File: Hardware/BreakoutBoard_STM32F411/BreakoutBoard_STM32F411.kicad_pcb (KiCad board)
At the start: 2 copper layers, 38 parts, among them IC101 STM32F411CCU6TR, IC401 TLV77333PDBVR, IC402 TLV77333PDBVR, J201 GSB1C41110SSHR, J202 PortB1, J203 PortB2, J204 PortA1, J205 PortA2, J206 SPI2, J207 PortA1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

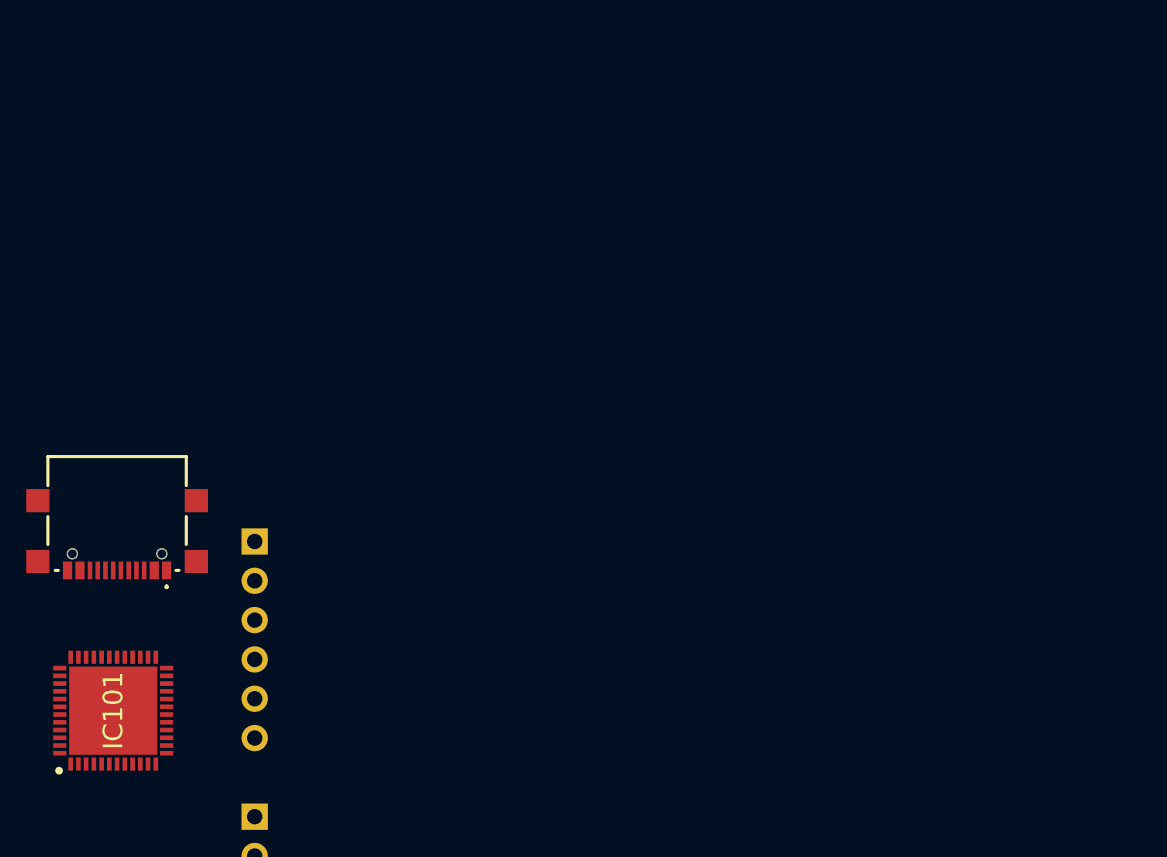
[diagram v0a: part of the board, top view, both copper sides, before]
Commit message: edited: default design rules
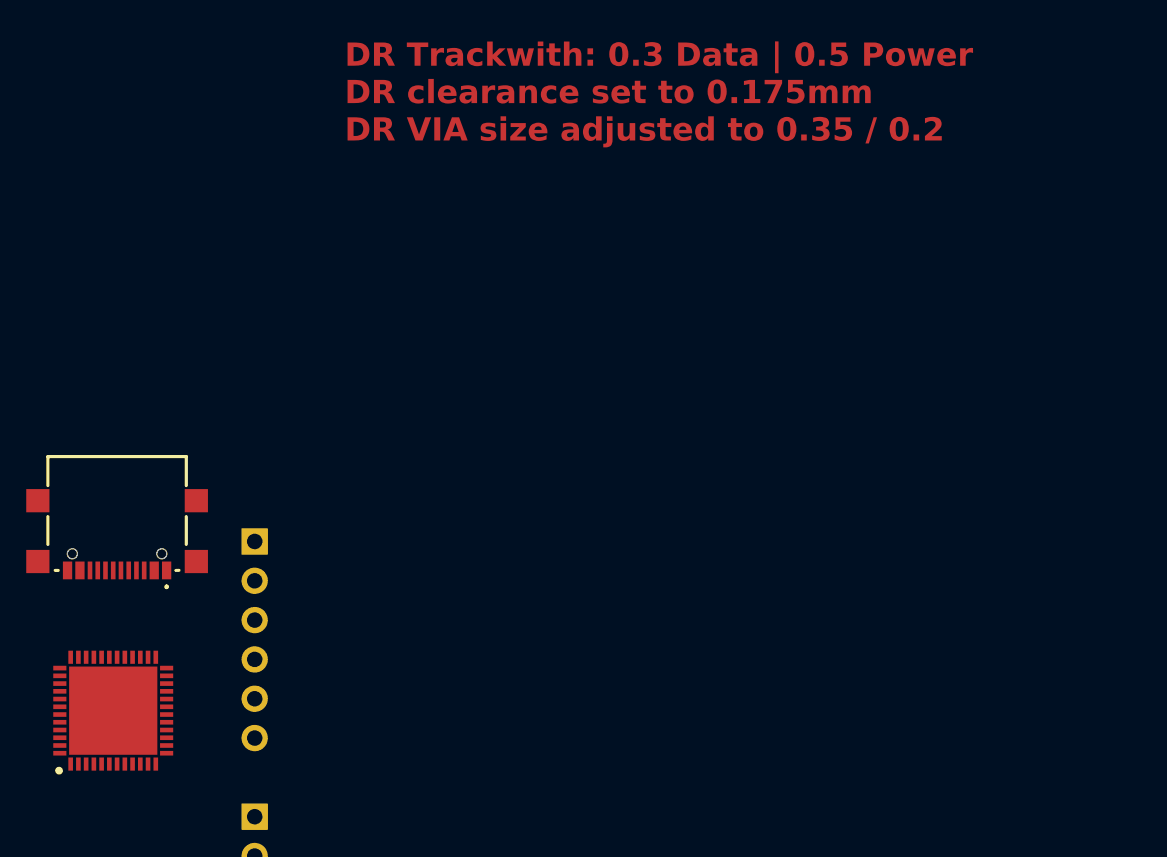
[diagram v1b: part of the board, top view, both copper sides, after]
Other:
- board text added: "DR Trackwith: 0.3 Data | 0.5 Power DR clearance set to 0.175mm DR VIA size adjusted to 0.35 / 0.2"
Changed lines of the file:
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@@
 	)
 	(setup
+		(stackup
+			(layer "F.SilkS"
+				(type "Top Silk Screen")
+			)
+			(layer "F.Paste"
+				(type "Top Solder Paste")
+			)
+			(layer "F.Mask"
+				(type "Top Solder Mask")
+				(thickness 0.01)
+			)
+			(layer "F.Cu"
+				(type "copper")
+				(thickness 0.035)
+			)
+			(layer "dielectric 1"
+				(type "core")
+				(thickness 1.51)
+				(material "FR4")
+				(epsilon_r 4.5)
+				(loss_tangent 0.02)
+			)
+			(layer "B.Cu"
+				(type "copper")
+				(thickness 0.035)
+			)
+			(layer "B.Mask"
+				(type "Bottom Solder Mask")
+				(thickness 0.01)
+			)
+			(layer "B.Paste"
+				(type "Bottom Solder Paste")
+			)
+			(layer "B.SilkS"
+				(type "Bottom Silk Screen")
+			)
+			(copper_finish "None")
+			(dielectric_constraints no)
+		)
 		(pad_to_mask_clearance 0)
 		(allow_soldermask_bridges_in_footprints no)
@@
 			(at 0 0 90)
 			(layer "F.SilkS")
+			(hide yes)
 			(effects
 				(font
@@
 		(layer "F.CrtYd")
 	)
+	(gr_text "DR Trackwith: 0.3 Data | 0.5 Power\nDR clearance set to 0.175mm\nDR VIA size adjusted to 0.35 / 0.2\n"
+		(at 139.7 26.8 0)
+		(layer "F.Cu")
+		(effects
+			(font
+				(size 1.5 1.5)
+				(thickness 0.3)
+				(bold yes)
+			)
+			(justify left bottom)
+		)
+	)
 	(embedded_fonts no)

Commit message: arranged:components (#3)
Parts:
- removed J206: SPI2, Connector_PinHeader_2.54mm:PinHeader_1x06_P2.54mm_Vertical
- removed J207: PortA1, Connector_PinHeader_2.54mm:PinHeader_1x06_P2.54mm_Vertical
- added J401: DeleteAfterPlacement1, Connector_PinHeader_2.54mm:PinHeader_1x06_P2.54mm_Vertical, F.Cu at (197.8, 42.9)
- added J402: DeleteAfterPlacement2, Connector_PinHeader_2.54mm:PinHeader_1x15_P2.54mm_Vertical, F.Cu at (180.8, 39.7)
- added J403: Conn_02x03_Odd_Even, Connector_PinHeader_2.54mm:PinHeader_2x03_P2.54mm_Vertical, F.Cu at (164.8, 147.9)
- added J404: SYS_JTAG, Connector_PinHeader_2.54mm:PinHeader_1x04_P2.54mm_Vertical, F.Cu at (158.4, 126.8)
- added J405: I2C2, Connector_PinHeader_2.54mm:PinHeader_1x04_P2.54mm_Vertical, B.Cu at (176.2, 126.8)
- moved LED701 134.0 mm to (166.0, 152.4)
- moved C701 131.9 mm to (166.1, 150.9)
- moved LED901 129.4 mm to (171.2, 152.4)
- moved C901 127.2 mm to (171.3, 150.9)
- moved C102 125.8 mm to (168.3, 138.1), turned to 180 degrees
- moved LED801 123.1 mm to (168.6, 152.4)
- moved C103 121.6 mm to (162.2, 139.6), turned to 90 degrees
- moved C801 120.9 mm to (168.7, 150.9)
- moved C106 118.3 mm to (171.8, 130.6), turned to -90 degrees
- moved C104 117.6 mm to (162.4, 136.3), turned to 90 degrees
- moved LED601 115.2 mm to (163.4, 152.4)
- moved Y101 113.8 mm to (165.0, 139.7)
- moved C601 112.8 mm to (163.5, 150.9)
- moved C101 111.6 mm to (168.9, 139.3)
- moved C105 111.5 mm to (172.8, 133.2), turned to 90 degrees
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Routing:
- net GND: track 0.00 -> 29.0 mm, vias 0 -> 24
- net +5V: track 0.00 -> 27.9 mm, vias 0 -> 20
- net PA11: track 0.00 -> 13.2 mm
- net +3.3V: track 0.00 -> 13.1 mm, vias 0 -> 11
- net PA12: track 0.00 -> 12.9 mm
- net DN: track 0.00 -> 9.24 mm, vias 0 -> 2
- net DP: track 0.00 -> 9.19 mm, vias 0 -> 2
- net /HMI_Debbug_4/AdrLED3/DO: track 0.00 -> 3.97 mm, vias 0 -> 2
- net /HMI_Debbug_4/AdrLED2/DO: track 0.00 -> 3.97 mm, vias 0 -> 2
- net /HMI_Debbug_4/AdrLED1/DO: track 0.00 -> 3.97 mm, vias 0 -> 2
- net Net-(IC101-VCAP_1): track 0.00 -> 2.45 mm
- net PH0: track 0.00 -> 2.33 mm
- net PA15 | TIM2_CH1: track 0.00 -> 1.25 mm, vias 0 -> 2
- net PB2: track 0.00 -> 1.10 mm, vias 0 -> 1
- net PB0: track 0.00 -> 1.10 mm, vias 0 -> 1
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- added copper zone on F.Cu, net +3.3V
- added copper zone on F.Cu, net +3.3VP
- added copper zone on F.Cu, net +5V
- added copper zone on B.Cu, net GND
- added copper zone on F.Cu, net GND
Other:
- board outline added: 21.4 x 50.1 mm
- board text added: "DR Trackwith: 0.3 Data | 0.5 Power DR clearance set to 0.175mm DR VIA size adjusted to 0.35 / 0.2 DR only using 0.1mm grid (0.5 if necessary)"
- board text added: "Die pins auf den PinHeadern gehören den umständen entsprächend getauscht!"
- board text removed: "DR Trackwith: 0.3 Data | 0.5 Power DR clearance set to 0.175mm DR VIA size adjusted to 0.35 / 0.2"

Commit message: routed PCB (#4)
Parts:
- D301: value LED -> 3.3V
- D302: value LED -> 5V
- moved D301 41.8 mm to (162.7, 124.5), turned to 90 degrees
- moved D302 38.8 mm to (160.3, 124.5), turned to 90 degrees
- moved R301 37.2 mm to (162.7, 121.5), turned to -90 degrees
- moved C501 35.9 mm to (165.3, 143.3), turned to 90 degrees
- moved R302 34.3 mm to (160.3, 121.5), turned to -90 degrees
- moved LED501 33.8 mm to (163.7, 143.2)
- moved J403 26.4 mm to (168.5, 121.8), turned to 0 degrees
- moved C403 22.5 mm to (170.4, 113.4)
- moved C404 22.5 mm to (170.4, 119.1)
- moved IC402 22.5 mm to (170.1, 116.2)
- moved C401 19.6 mm to (161.0, 113.4)
- moved C402 19.6 mm to (161.0, 119.1)
- moved IC401 19.6 mm to (160.7, 116.2)
- moved C101 2.07 mm to (167.4, 140.7)
- moved C102 2.07 mm to (166.8, 139.5)
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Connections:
- J203 pad 5: PA8 -> PB0
- J203 pad 6: PA9 -> PB1
- J204 pad 1: PB0 -> PA8
- J204 pad 2: PB1 -> PA9
- J204 pad 3: PB2 -> PA10
- J204 pad 4: PB3 -> PB4
- J204 pad 5: PB4 -> PB3
- J403 pad 1: +3.3VP -> PB15 | SPI2_MOSI
- J403 pad 3: PB13 | SPI2_SCK -> PB14 | SPI2_MISO
- J403 pad 4: PB15 | SPI2_MOSI -> PB13 | SPI2_SCK
- J403 pad 6: PB14 | SPI2_MISO -> +3.3VP
- J404 pad 1: PA14 | SYS_SWCLK -> PA13 | SYS_SWDIO
- J404 pad 2: PA13 | SYS_SWDIO -> PA14 | SYS_SWCLK
- J405 pad 1: PB10 | I2C2_SCL -> +5V
- J405 pad 2: PB9 | I2C2_SDA -> GND
- J405 pad 4: +3.3V -> +3.3VP
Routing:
- net +5V: track 27.9 -> 110.8 mm, vias 20 -> 7
- net +3.3V: track 13.1 -> 69.9 mm, vias 11 -> 14
- net +3.3VP: track 0.00 -> 46.2 mm, vias 6 -> 8
- net PB3: track 0.00 -> 30.4 mm, vias 0 -> 1
- net PB4: track 0.00 -> 29.1 mm, vias 0 -> 1
- net PA4: track 0.00 -> 27.3 mm
- net PA0: track 0.00 -> 26.5 mm
- net PA1: track 0.00 -> 25.4 mm
- net PA3: track 0.00 -> 25.2 mm
- net PA2: track 0.00 -> 24.2 mm
- net PB5: track 0.00 -> 22.3 mm, vias 0 -> 1
- net PA10: track 0.00 -> 20.8 mm, vias 0 -> 1
- net PB7: track 0.00 -> 20.5 mm, vias 0 -> 1
- net PB6: track 0.00 -> 20.4 mm, vias 0 -> 1
- net PA8: track 0.00 -> 19.5 mm, vias 0 -> 1
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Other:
- board text added: "DRC fehler überprüfen"
- board text removed: "Die pins auf den PinHeadern gehören den umständen entsprächend getauscht!"

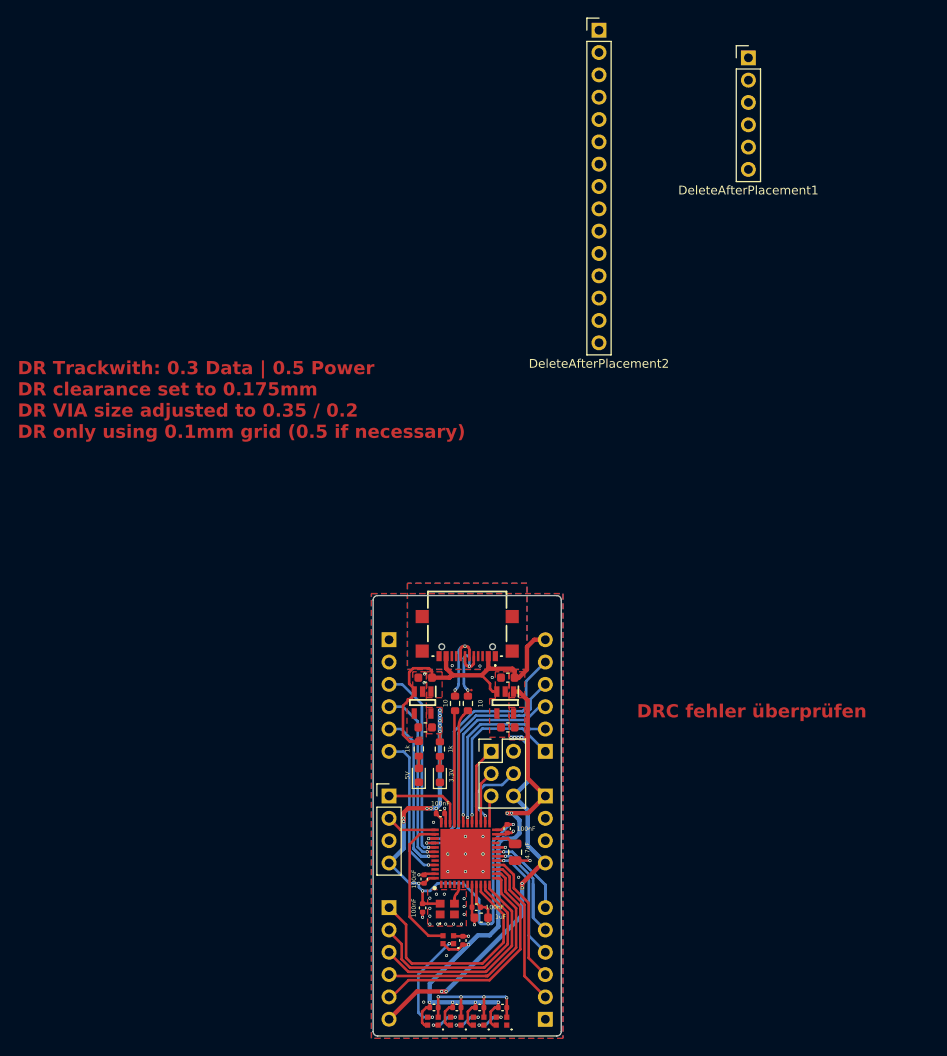
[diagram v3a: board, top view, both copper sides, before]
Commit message: fixed:Viasize, fixed:NRST and BOOT0 (#5)
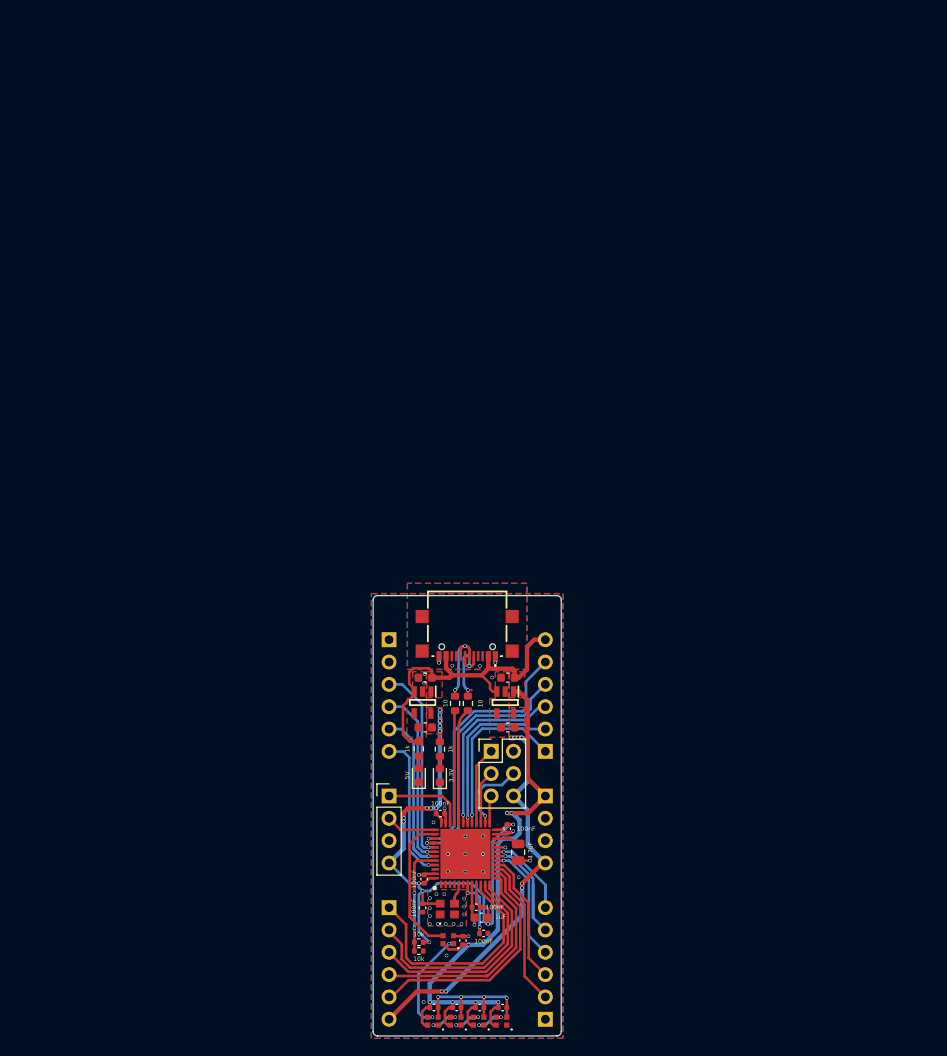
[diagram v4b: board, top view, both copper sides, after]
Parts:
- removed J401: DeleteAfterPlacement1, Connector_PinHeader_2.54mm:PinHeader_1x06_P2.54mm_Vertical
- removed J402: DeleteAfterPlacement2, Connector_PinHeader_2.54mm:PinHeader_1x15_P2.54mm_Vertical
- added C405: 100nF, Capacitor_SMD:C_0402_1005Metric, F.Cu at (167.7, 142.5)
- added R401: 10k, Resistor_SMD:R_0402_1005Metric, F.Cu at (160.3, 143.5)
- added R402: 10k, Resistor_SMD:R_0402_1005Metric, F.Cu at (160.3, 144.5)
- moved C105 0.34 mm to (171.6, 133.3)
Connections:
- IC101 pad 44: unconnected-(IC101-BOOT0-Pad44) -> BOOT0
- IC101 pad 7: unconnected-(IC101-NRST-Pad7) -> NRST
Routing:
- net BOOT0: track 0.00 -> 12.5 mm, vias 0 -> 2
- net +3.3V: track 69.9 -> 77.2 mm, vias 14 -> 15
- net NRST: track 0.00 -> 6.67 mm, vias 0 -> 2
- net Net-(IC101-VCAP_1): track 2.45 -> 3.14 mm
- net GND: track 31.2 -> 31.7 mm, vias 41 -> 42
- added copper zone on In1.Cu, net GND
- added copper zone on In2.Cu, net GND
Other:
- copper layers 2 -> 4
- board text added: "DR Trackwith: 0.3 Data | 0.5 Power DR clearance set to 0.175mm DR VIA size adjusted to 0.3 / 0.4 DR only using 0.1mm grid (0.5 if necessary)"
- board text added: "replaced all vias with 0.3 / 0.4 and look DRC"
- board text removed: "DR Trackwith: 0.3 Data | 0.5 Power DR clearance set to 0.175mm DR VIA size adjusted to 0.35 / 0.2 DR only using 0.1mm grid (0.5 if necessary)"
- board text removed: "DRC fehler überprüfen"

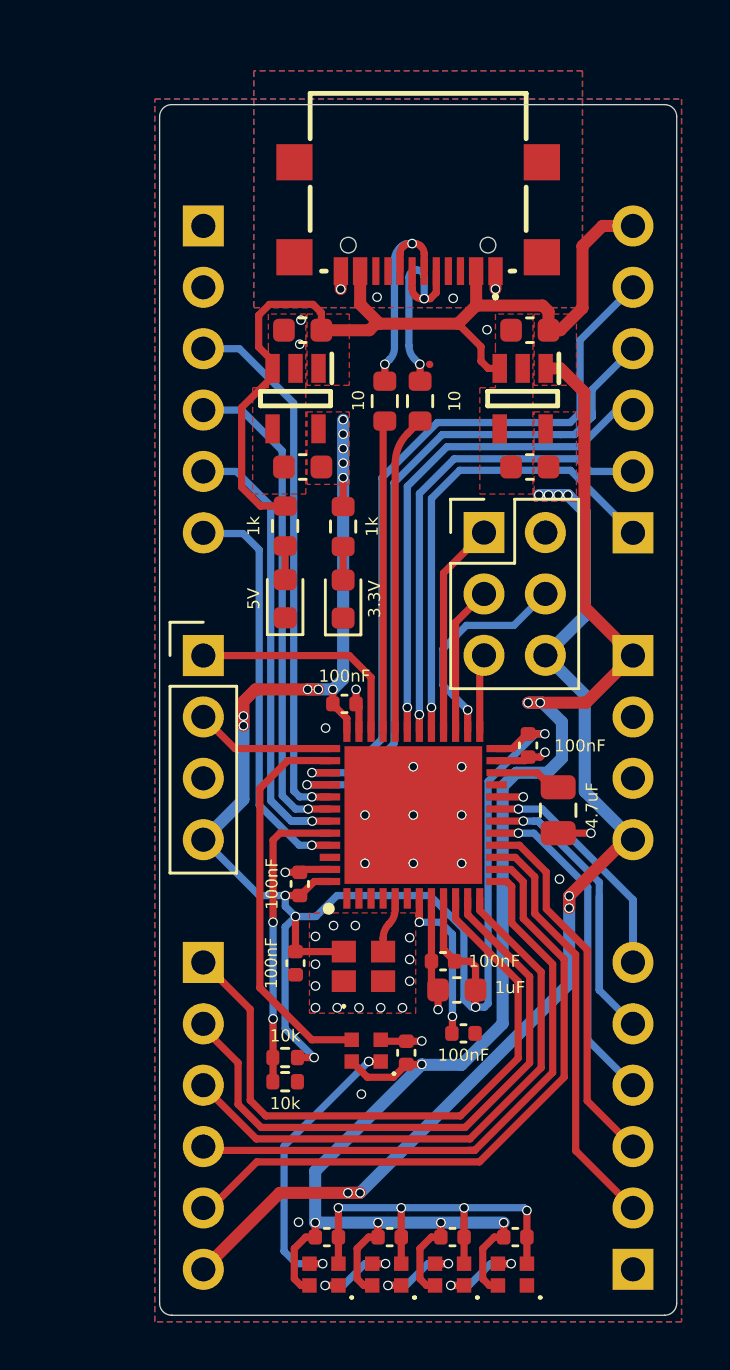
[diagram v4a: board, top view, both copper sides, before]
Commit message: fixed:Via size, fixed:DRC, edited:Silkscreen (#6)
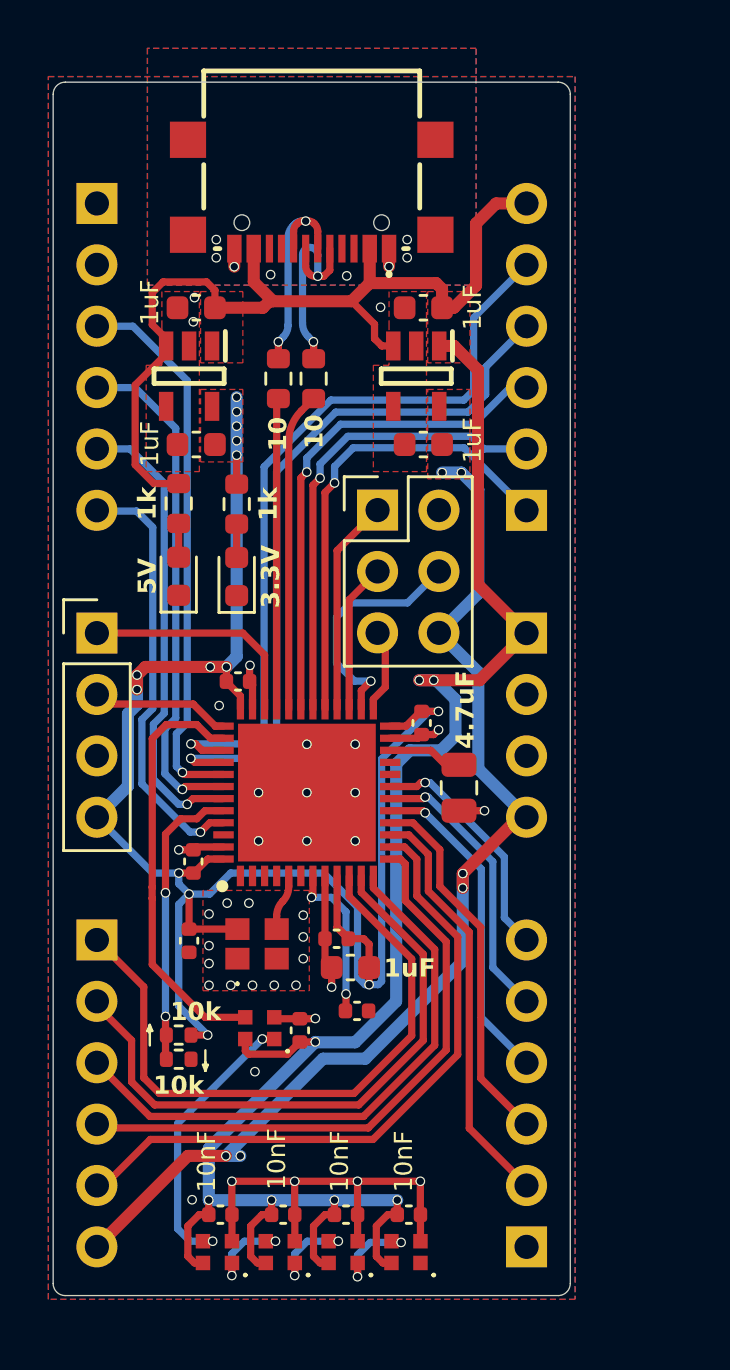
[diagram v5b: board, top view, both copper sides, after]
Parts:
- moved C101 4.50 mm to (163.0, 139.8)
- moved C102 4.50 mm to (162.4, 138.6)
- moved C103 4.50 mm to (156.3, 138.7)
- moved C104 4.50 mm to (156.5, 135.4)
- moved C106 4.50 mm to (165.9, 129.7)
- moved C107 4.50 mm to (158.3, 127.9)
- moved C401 4.50 mm to (156.6, 112.5)
- moved C402 4.50 mm to (156.6, 118.1)
- moved C403 4.50 mm to (166.0, 112.5)
- moved C404 4.50 mm to (166.0, 118.1)
- moved C405 4.50 mm to (163.3, 141.6)
- moved C501 4.50 mm to (160.9, 142.4)
- moved C601 4.50 mm to (157.6, 150.0)
- moved C701 4.50 mm to (160.2, 150.0)
- moved C801 4.50 mm to (162.8, 150.0)
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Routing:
- net PB0: track 16.3 -> 11.7 mm
- net PB1: track 12.4 -> 9.88 mm
- net PA15 | TIM2_CH1: track 16.3 -> 17.5 mm
- net PB3: track 30.4 -> 31.6 mm
- net PB2: track 1.10 -> 0.00 mm, vias 1 -> 0
- net PB7: track 20.5 -> 19.5 mm
- net PB13 | SPI2_SCK: track 9.03 -> 9.98 mm
- net PB8: track 16.8 -> 17.7 mm
- net PB6: track 20.4 -> 21.2 mm
- net PA10: track 20.8 -> 20.1 mm
- net PB4: track 29.1 -> 29.7 mm
- net Net-(IC101-VCAP_1): track 3.14 -> 2.53 mm
- net PB5: track 22.3 -> 22.9 mm
- net PA14 | SYS_SWCLK: track 5.78 -> 5.22 mm
- net +3.3VP: track 46.2 -> 45.7 mm, vias 8 -> 6
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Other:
- board size 21.4 x 50.1 mm -> 21.4 x 50.2 mm
- board text removed: "replaced all vias with 0.3 / 0.4 and look DRC"
